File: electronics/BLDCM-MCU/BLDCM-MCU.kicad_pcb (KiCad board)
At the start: 4 copper layers, 32 x 32 mm, 85 parts, among them J1 52991-0308, K1 EVPAKE31A, U1 STM32F446RE, U10 SK6805, U11 SK6805, U12 SK6805, U13 SK6805, U14 SK6805, U15 SK6805, U16 SK6805, U17 SK6805, U18 SK6805, U19 SK6805, U2 SN74LV1T34DBVR, U20 MT6701, U3 ISM330DHCX, U4 SK6805, U5 SK6805, U6 SK6805, U7 SK6805, U8 SK6805, U9 SK6805, Y1 ECS-3225MVLC-240-CN

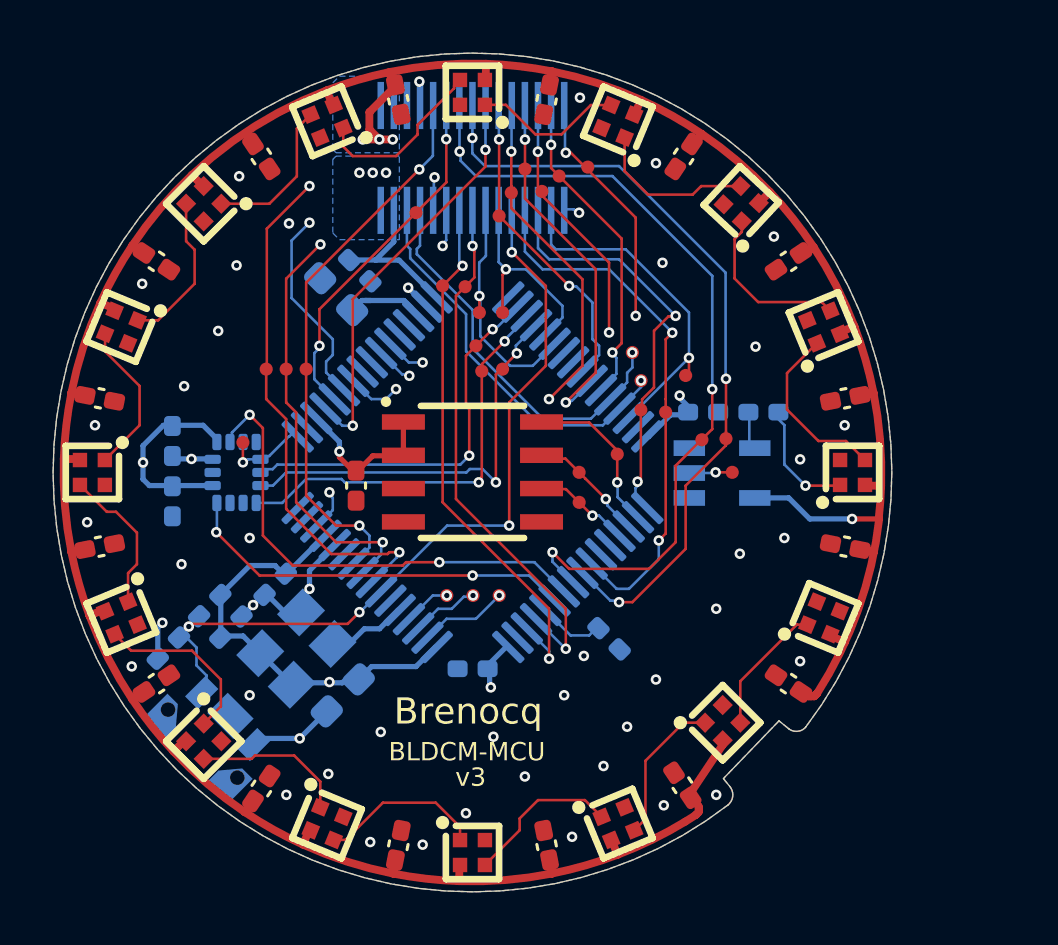
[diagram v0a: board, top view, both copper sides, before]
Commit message: Feat: Attach MCU PCB to motor
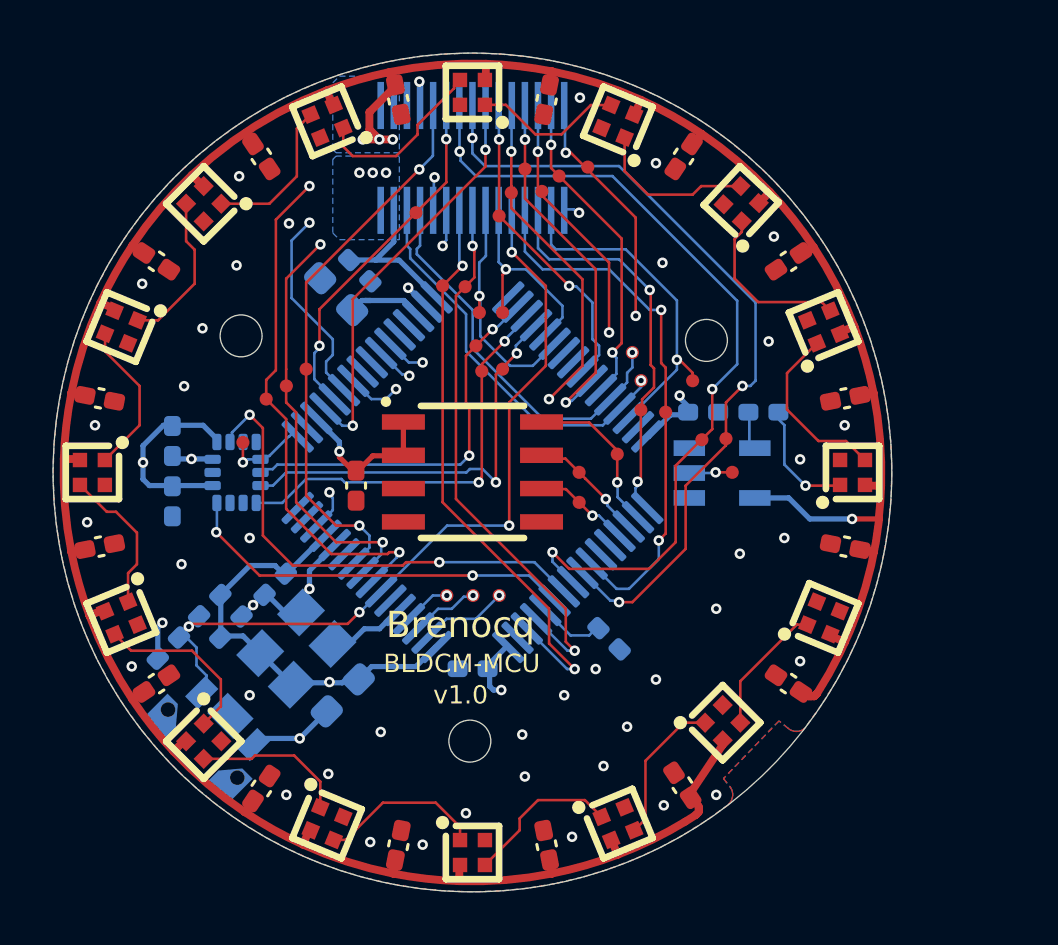
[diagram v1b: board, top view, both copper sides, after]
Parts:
- moved TP3 1.14 mm to (140.6, 102.2)
- moved TP5 0.64 mm to (141.4, 101.7)
- moved TP26 0.33 mm to (156.9, 101.5)
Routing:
- net /CAN.TX: track 20.7 -> 22.4 mm
- net /INA.POCI: track 29.8 -> 30.9 mm
- net /SWCLK: track 16.1 -> 15.2 mm
- net /INA.PICO: track 31.1 -> 31.9 mm
- net /CAN.RX: track 20.4 -> 21.0 mm
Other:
- outline, holes or cut-outs redrawn
- board text added: "v1.0"
- board text removed: "v3"

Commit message: Refactor(pcb): Rename VIN to 5V in MCU PCB
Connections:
- net VIN renamed 5V
- K1 pad NC: (no net) -> unconnected-(K1-PadNC)_5
- U2 pad 1: (no net) -> unconnected-(U2-NC-Pad1)
- U3 pad 10: (no net) -> unconnected-(U3-OCS_Aux-Pad10)
- U3 pad 11: (no net) -> unconnected-(U3-SDO_Aux-Pad11)
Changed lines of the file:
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@@
 	(property "SHEETTOTAL" "1")
 	(net 0 "")
-	(net 1 "VIN")
+	(net 1 "5V")
 	(net 2 "GND")
 	(net 3 "3.3V")
@@
 	(net 75 "unconnected-(U20-PUSH-Pad5)")
 	(net 76 "unconnected-(U20-OUT-Pad3)")
+	(net 77 "unconnected-(K1-PadNC)")
+	(net 78 "unconnected-(U2-NC-Pad1)")
+	(net 79 "unconnected-(U3-OCS_Aux-Pad10)")
+	(net 80 "unconnected-(U3-SDO_Aux-Pad11)")
+	(net 81 "unconnected-(K1-PadNC)_1")
+	(net 82 "unconnected-(K1-PadNC)_2")
+	(net 83 "unconnected-(K1-PadNC)_3")
+	(net 84 "unconnected-(K1-PadNC)_4")
+	(net 85 "unconnected-(K1-PadNC)_5")
+	(net 86 "unconnected-(K1-PadNC)_6")
 	(footprint "BrenoCQ:TP_0.5mm"
 		(layer "F.Cu")
@@
 			(size 0.55 0.55)
 			(layers "F.Cu" "F.Mask" "F.Paste")
-			(net 1 "VIN")
+			(net 1 "5V")
 			(pinfunction "VDD")
 			(pintype "passive")
@@
 			(layers "F.Cu" "F.Mask" "F.Paste")
 			(roundrect_rratio 0.25)
-			(net 1 "VIN")
+			(net 1 "5V")
 			(pinfunction "2")
 			(pintype "passive")
@@
 			(layers "F.Cu" "F.Mask" "F.Paste")
 			(roundrect_rratio 0.25)
-			(net 1 "VIN")
+			(net 1 "5V")
 			(pinfunction "2")
 			(pintype "passive")
@@
 			(size 0.55 0.55)
 			(layers "F.Cu" "F.Mask" "F.Paste")
-			(net 1 "VIN")
+			(net 1 "5V")
 			(pinfunction "VDD")
 			(pintype "passive")
@@
 			(size 0.55 0.55)
 			(layers "F.Cu" "F.Mask" "F.Paste")
-			(net 1 "VIN")
+			(net 1 "5V")
 			(pinfunction "VDD")
 			(pintype "passive")
@@
 			(size 0.55 0.55)
 			(layers "F.Cu" "F.Mask" "F.Paste")
-			(net 1 "VIN")
+			(net 1 "5V")
 			(pinfunction "VDD")
 			(pintype "passive")
@@
 			(layers "F.Cu" "F.Mask" "F.Paste")
 			(roundrect_rratio 0.25)
-			(net 1 "VIN")
+			(net 1 "5V")
 			(pinfunction "2")
 			(pintype "passive")
@@
 			(layers "F.Cu" "F.Mask" "F.Paste")
 			(roundrect_rratio 0.25)
-			(net 1 "VIN")
+			(net 1 "5V")
 			(pinfunction "2")
 			(pintype "passive")
@@
 			(size 0.55 0.55)
 			(layers "F.Cu" "F.Mask" "F.Paste")
-			(net 1 "VIN")
+			(net 1 "5V")
 			(pinfunction "VDD")
 			(pintype "passive")
@@
 			(size 0.55 0.55)
 			(layers "F.Cu" "F.Mask" "F.Paste")
-			(net 1 "VIN")
+			(net 1 "5V")
 			(pinfunction "VDD")
 			(pintype "passive")
@@
 			(layers "F.Cu" "F.Mask" "F.Paste")
 			(roundrect_rratio 0.25)
-			(net 1 "VIN")
+			(net 1 "5V")
 			(pinfunction "2")
 			(pintype "passive")
@@
 			(layers "F.Cu" "F.Mask" "F.Paste")
 			(roundrect_rratio 0.25)
-			(net 1 "VIN")
+			(net 1 "5V")
 			(pinfunction "2")
 			(pintype "passive")
@@
 			(layers "F.Cu" "F.Mask" "F.Paste")
 			(roundrect_rratio 0.25)
-			(net 1 "VIN")
+			(net 1 "5V")
 			(pinfunction "2")
 			(pintype "passive")
@@
 			(size 0.55 0.55)
 			(layers "F.Cu" "F.Mask" "F.Paste")
-			(net 1 "VIN")
+			(net 1 "5V")
 			(pinfunction "VDD")
 			(pintype "passive")
@@
 			(layers "F.Cu" "F.Mask" "F.Paste")
 			(roundrect_rratio 0.25)
-			(net 1 "VIN")
+			(net 1 "5V")
 			(pinfunction "2")
 			(pintype "passive")
@@
 			(size 0.55 0.55)
 			(layers "F.Cu" "F.Mask" "F.Paste")
-			(net 1 "VIN")
+			(net 1 "5V")
 			(pinfunction "VDD")
 			(pintype "passive")
@@
 			(layers "F.Cu" "F.Mask" "F.Paste")
 			(roundrect_rratio 0.25)
-			(net 1 "VIN")
+			(net 1 "5V")
 			(pinfunction "2")
 			(pintype "passive")
@@
 			(size 0.55 0.55)
 			(layers "F.Cu" "F.Mask" "F.Paste")
-			(net 1 "VIN")
+			(net 1 "5V")
 			(pinfunction "VDD")
 			(pintype "passive")
@@
 			(layers "F.Cu" "F.Mask" "F.Paste")
 			(roundrect_rratio 0.25)
-			(net 1 "VIN")
+			(net 1 "5V")
 			(pinfunction "2")
 			(pintype "passive")
@@
 			(size 0.55 0.55)
 			(layers "F.Cu" "F.Mask" "F.Paste")
-			(net 1 "VIN")
+			(net 1 "5V")
 			(pinfunction "VDD")
 			(pintype "passive")
@@
 			(size 0.55 0.55)
 			(layers "F.Cu" "F.Mask" "F.Paste")
-			(net 1 "VIN")
+			(net 1 "5V")
 			(pinfunction "VDD")
 			(pintype "passive")
@@
 			(layers "F.Cu" "F.Mask" "F.Paste")
 			(roundrect_rratio 0.25)
-			(net 1 "VIN")
+			(net 1 "5V")
 			(pinfunction "2")
 			(pintype "passive")
@@
 			(layers "F.Cu" "F.Mask" "F.Paste")
 			(roundrect_rratio 0.25)
-			(net 1 "VIN")
+			(net 1 "5V")
 			(pinfunction "2")
 			(pintype "passive")
@@
 			(size 0.55 0.55)
 			(layers "F.Cu" "F.Mask" "F.Paste")
-			(net 1 "VIN")
+			(net 1 "5V")
 			(pinfunction "VDD")
 			(pintype "passive")
@@
 			(size 0.55 0.55)
 			(layers "F.Cu" "F.Mask" "F.Paste")
-			(net 1 "VIN")
+			(net 1 "5V")
 			(pinfunction "VDD")
 			(pintype "passive")
@@
 			(size 0.55 0.55)
 			(layers "F.Cu" "F.Mask" "F.Paste")
-			(net 1 "VIN")
+			(net 1 "5V")
 			(pinfunction "VDD")
 			(pintype "passive")
@@
 			(layers "F.Cu" "F.Mask" "F.Paste")
 			(roundrect_rratio 0.25)
-			(net 1 "VIN")
+			(net 1 "5V")
 			(pinfunction "2")
 			(pintype "passive")
@@
 			(layers "F.Cu" "F.Mask" "F.Paste")
 			(roundrect_rratio 0.25)
-			(net 1 "VIN")
+			(net 1 "5V")
 			(pinfunction "2")
 			(pintype "passive")
@@
 			(size 0.55 0.55)
 			(layers "F.Cu" "F.Mask" "F.Paste")
-			(net 1 "VIN")
+			(net 1 "5V")
 			(pinfunction "VDD")
 			(pintype "passive")
@@
 			(layers "F.Cu" "F.Mask" "F.Paste")
 			(roundrect_rratio 0.25)
-			(net 1 "VIN")
+			(net 1 "5V")
 			(pinfunction "2")
 			(pintype "passive")
@@
 			(layers "F.Cu" "F.Mask" "F.Paste")
 			(roundrect_rratio 0.25)
-			(net 1 "VIN")
+			(net 1 "5V")
 			(pinfunction "2")
 			(pintype "passive")
@@
 			(size 0.55 0.55)
 			(layers "F.Cu" "F.Mask" "F.Paste")
-			(net 1 "VIN")
+			(net 1 "5V")
 			(pinfunction "VDD")
 			(pintype "passive")
@@
 			(size 1.2 0.6)
 			(layers "B.Cu" "B.Mask" "B.Paste")
+			(net 78 "unconnected-(U2-NC-Pad1)")
+			(pinfunction "NC")
+			(pintype "passive")
 		)
 		(pad "2" smd rect
@@
 			(size 1.2 0.6)
 			(layers "B.Cu" "B.Mask" "B.Paste")
-			(net 1 "VIN")
+			(net 1 "5V")
 			(pinfunction "VCC")
 			(pintype "passive")
@@
 			(layers "B.Cu" "B.Mask" "B.Paste")
 			(roundrect_rratio 0.25)
+			(net 79 "unconnected-(U3-OCS_Aux-Pad10)")
+			(pinfunction "OCS_Aux")
+			(pintype "no_connect")
 		)
 		(pad "11" smd roundrect
@@
 			(layers "B.Cu" "B.Mask" "B.Paste")
 			(roundrect_rratio 0.25)
+			(net 80 "unconnected-(U3-SDO_Aux-Pad11)")
+			(pinfunction "SDO_Aux")
+			(pintype "no_connect")
 		)
 		(pad "12" smd roundrect
@@
 			(size 1.1 1.4)
 			(layers "B.Cu" "B.Mask" "B.Paste")
+			(net 77 "unconnected-(K1-PadNC)")
+			(pinfunction "NC")
+			(pintype "no_connect")
 		)
 		(pad "NC" thru_hole circle
@@
 			(layers "F&B.Cu" "*.Mask")
 			(remove_unused_layers no)
+			(net 86 "unconnected-(K1-PadNC)_6")
+			(pinfunction "NC")
+			(pintype "no_connect")
 			(thermal_bridge_angle 90)
 		)
@@
 			(size 0.0254 0.0254)
 			(layers "B.Cu" "B.Mask" "B.Paste")
+			(net 84 "unconnected-(K1-PadNC)_4")
+			(pinfunction "NC")
+			(pintype "no_connect")
 			(thermal_bridge_angle 90)
 		)
@@
 			(size 0.0254 0.0254)
 			(layers "B.Cu" "B.Mask" "B.Paste")
+			(net 82 "unconnected-(K1-PadNC)_2")
+			(pinfunction "NC")
+			(pintype "no_connect")
 			(thermal_bridge_angle 90)
 		)
@@
 			(layers "F&B.Cu" "*.Mask")
 			(remove_unused_layers no)
+			(net 83 "unconnected-(K1-PadNC)_3")
+			(pinfunction "NC")
+			(pintype "no_connect")
 			(thermal_bridge_angle 90)
 		)
@@
 			(size 0.000001 0.000001)
 			(layers "B.Cu" "B.Mask" "B.Paste")
+			(net 81 "unconnected-(K1-PadNC)_1")
+			(pinfunction "NC")
+			(pintype "no_connect")
 			(solder_mask_margin 0.075)
 			(solder_paste_margin 0.000001)
@@
 			(size 0.000001 0.000001)
 			(layers "B.Cu" "B.Mask" "B.Paste")
+			(net 85 "unconnected-(K1-PadNC)_5")
+			(pinfunction "NC")
+			(pintype "no_connect")
 			(solder_mask_margin 0.075)
 			(solder_paste_margin 0.000001)
@@
 			(size 1.8 0.25)
 			(layers "B.Cu" "B.Mask" "B.Paste")
-			(net 1 "VIN")
+			(net 1 "5V")
 			(pinfunction "2")
 			(pintype "passive")
@@
 			(size 1.8 0.25)
 			(layers "B.Cu" "B.Mask" "B.Paste")
-			(net 1 "VIN")
+			(net 1 "5V")
 			(pinfunction "4")
 			(pintype "passive")
@@
 	(zone
 		(net 1)
-		(net_name "VIN")
+		(net_name "5V")
 		(layer "B.Cu")
 		(hatch edge 0.5)

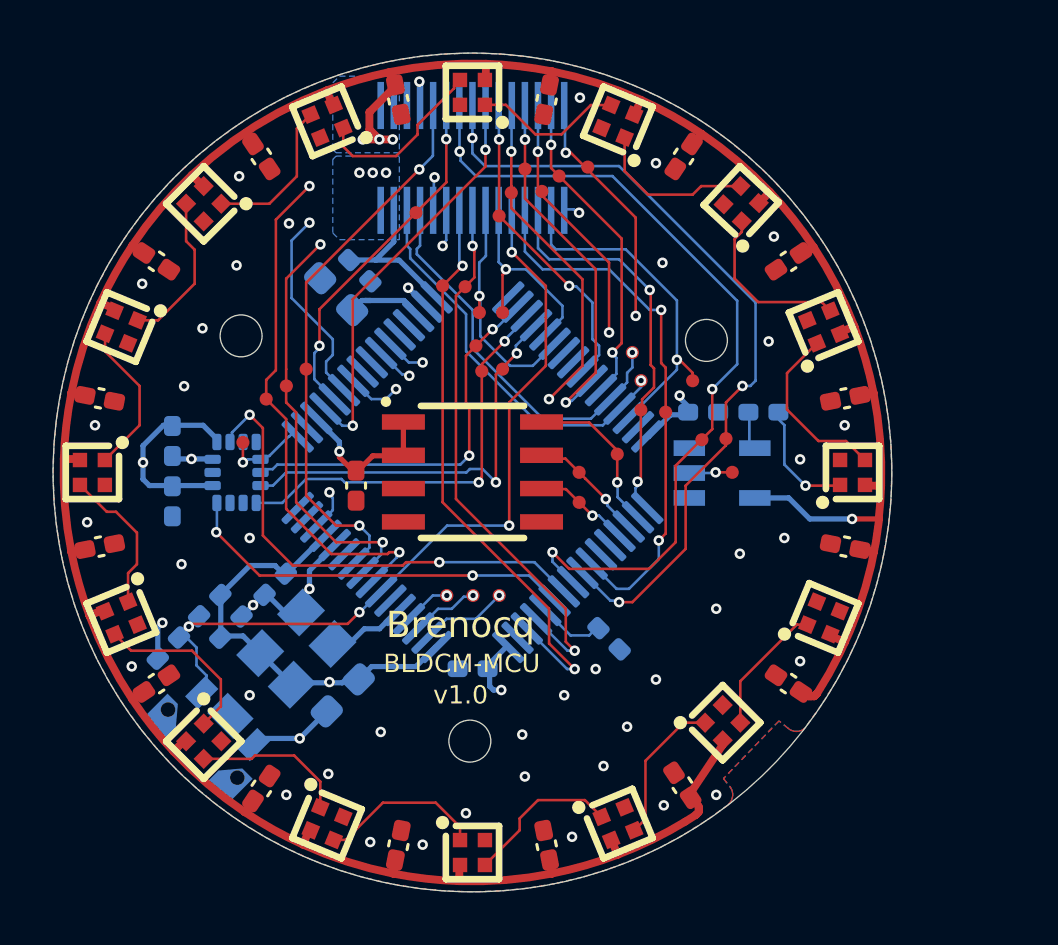
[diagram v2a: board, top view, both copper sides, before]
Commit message: Feat(pcb): Route current sense
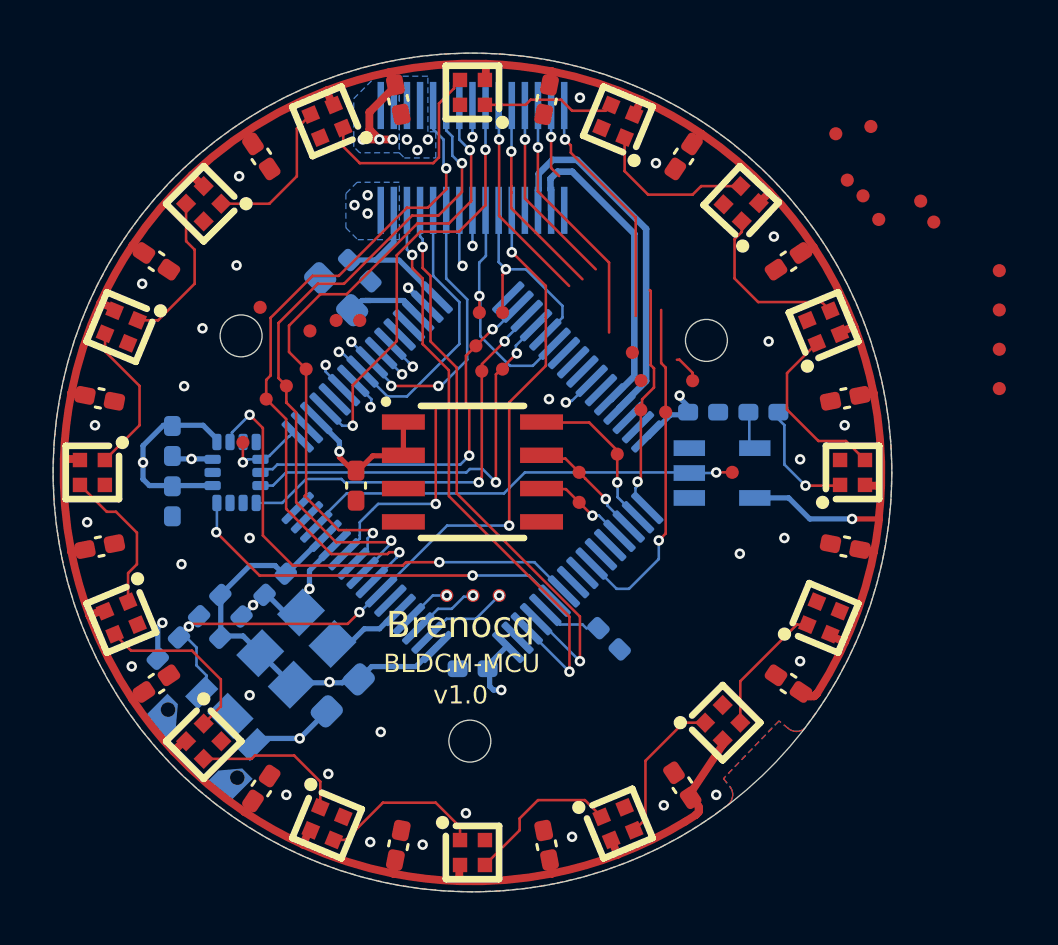
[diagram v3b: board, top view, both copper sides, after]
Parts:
- added TP25: Test point 0.5mm, BrenoCQ:TP_0.5mm, F.Cu at (168.6, 97.3)
- added TP34: Test point 0.5mm, BrenoCQ:TP_0.5mm, F.Cu at (168.6, 98.8)
- added TP35: Test point 0.5mm, BrenoCQ:TP_0.5mm, F.Cu at (168.6, 100.3)
- added TP36: Test point 0.5mm, BrenoCQ:TP_0.5mm, F.Cu at (168.6, 101.8)
- moved TP9 18.5 mm to (140.4, 98.7)
- moved TP16 16.6 mm to (163.7, 91.8)
- moved TP15 16.6 mm to (166.1, 95.5)
- moved TP18 16.1 mm to (162.4, 92.1)
- moved TP11 13.8 mm to (144.2, 99.2)
- moved TP17 13.6 mm to (164.0, 95.4)
- moved TP4 12.8 mm to (165.6, 94.7)
- moved TP2 12.3 mm to (163.4, 94.5)
- moved TP19 11.0 mm to (162.8, 93.9)
- moved TP13 9.32 mm to (142.3, 99.6)
- moved TP10 5.12 mm to (143.3, 99.2)
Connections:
- net /TCM.DIAG renamed /TMC.DIAG
- J1 pad 10: /INA.CS2 -> /CURR.U
- J1 pad 11: /INA.CS1 -> /VOLT.W
- J1 pad 12: /INA.CLK -> /CURR.V
- J1 pad 13: /CAN.TX -> /VCP.RX
- J1 pad 14: /INA.PICO -> /CURR.W
- J1 pad 15: /CAN.RX -> /VCP.TX
- J1 pad 16: /INA.POCI -> /VOLT.U
- J1 pad 17: /VCP.RX -> /RST
- J1 pad 19: /VCP.TX -> /SWO
- J1 pad 21: /RST -> /SWCLK
- J1 pad 23: /SWO -> /SWDIO
- J1 pad 25: /SWCLK -> /USB.DP
- J1 pad 27: /SWDIO -> /USB.DN
- J1 pad 29: /VOLT -> /VOLT.SRC
- J1 pad 5: /USB_P -> /CAN.TX
- J1 pad 7: /USB_N -> /CAN.RX
- J1 pad 9: /INA.CS0 -> /VOLT.V
- TP10 pad 1: /INA.CLK -> /VOLT.V
- TP11 pad 1: /INA.PICO -> /VOLT.W
- TP13 pad 1: /TMC.UL -> /VOLT.SRC
- TP15 pad 1: /TMC.UH -> /TMC.UL
- TP17 pad 1: /TMC.VH -> /TMC.UH
- TP19 pad 1: /TMC.WH -> /TMC.VH
- TP21 pad 1: /USB_N -> /TMC.WH
- TP23 pad 1: /USB_P -> /USB.DN
- TP26 pad 1: /SWDIO -> /USB.DP
- TP29 pad 1: /SWCLK -> /SWDIO
- TP3 pad 1: /INA.CS0 -> /CURR.U
- TP32 pad 1: /ENC.CS -> /SWCLK
- TP5 pad 1: /INA.CS1 -> /CURR.V
- TP6 pad 1: /INA.CS2 -> /CURR.W
- TP9 pad 1: /INA.POCI -> /VOLT.U
- U1 pad 10: /INA.CS2 -> /CURR.W
- U1 pad 11: unconnected-(U1C-PC3-Pad11) -> /VOLT.U
- U1 pad 21: /INA.CLK -> unconnected-(U1A-PA5-Pad21)
- U1 pad 22: /VOLT -> /VOLT.SRC
- U1 pad 24: unconnected-(U1C-PC4-Pad24) -> /VOLT.V
- U1 pad 25: unconnected-(U1C-PC5-Pad25) -> /VOLT.W
- U1 pad 44: /USB_N -> /USB.DN
- U1 pad 45: /USB_P -> /USB.DP
- U1 pad 56: /INA.POCI -> unconnected-(U1B-PB4-Pad56)
- U1 pad 57: /INA.PICO -> unconnected-(U1B-PB5-Pad57)
- U1 pad 8: /INA.CS0 -> /CURR.U
- U1 pad 9: /INA.CS1 -> /CURR.V
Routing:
- net /INA.PICO: track 31.9 -> 0.00 mm, vias 3 -> 0
- net /INA.POCI: track 30.9 -> 0.00 mm, vias 3 -> 0
- net /CURR.U: track 0.00 -> 26.5 mm, vias 0 -> 2
- net /INA.CS0: track 26.2 -> 0.00 mm, vias 3 -> 0
- net /CURR.V: track 0.00 -> 25.8 mm, vias 0 -> 2
- net /CURR.W: track 0.00 -> 24.2 mm, vias 0 -> 2
- net /INA.CS1: track 22.1 -> 0.00 mm, vias 3 -> 0
- net /INA.CS2: track 21.3 -> 0.00 mm, vias 2 -> 0
- net /VOLT: track 18.9 -> 0.00 mm, vias 2 -> 0
- net /USB.DP: track 0.00 -> 15.2 mm
- net /USB_P: track 15.0 -> 0.00 mm, vias 1 -> 0
- net /USB_N: track 15.0 -> 0.00 mm, vias 1 -> 0
- net /INA.CLK: track 13.6 -> 0.00 mm, vias 2 -> 0
- net /SWDIO: track 13.3 -> 0.00 mm, vias 1 -> 0
- net /USB.DN: track 0.00 -> 12.2 mm
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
